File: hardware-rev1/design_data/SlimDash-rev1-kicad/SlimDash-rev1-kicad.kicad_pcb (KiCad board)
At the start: 2 copper layers, 157.1 x 131.5 mm, 70 parts

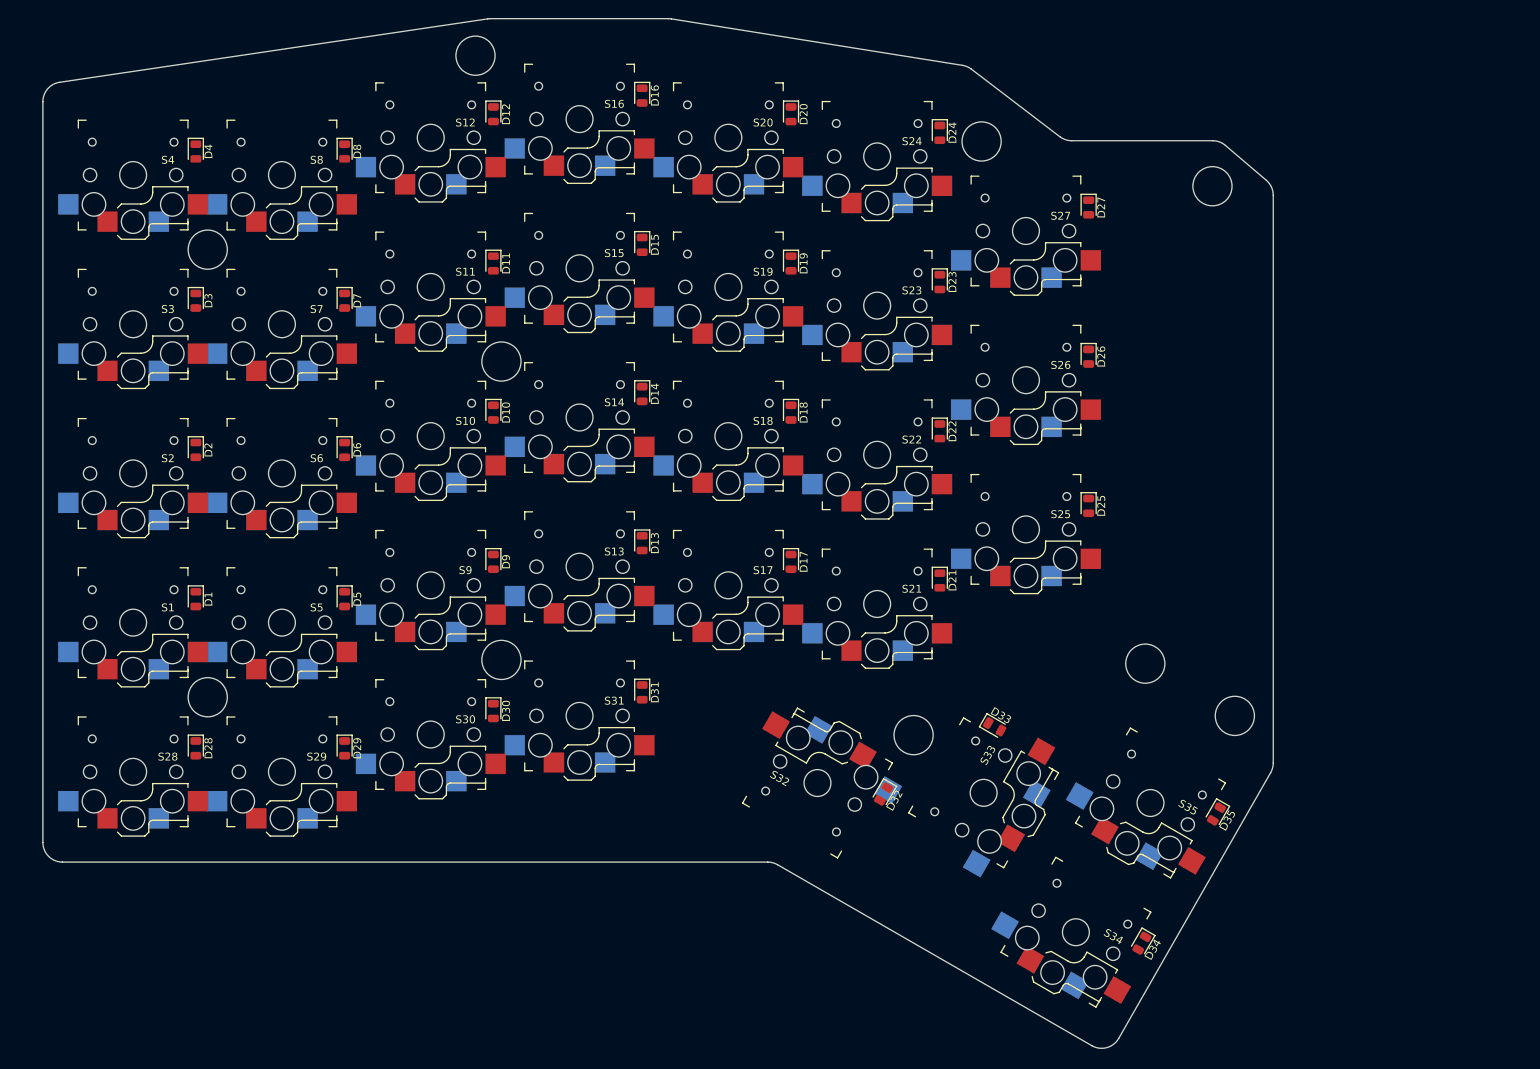
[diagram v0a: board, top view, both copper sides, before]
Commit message: fix some positioning and net labels
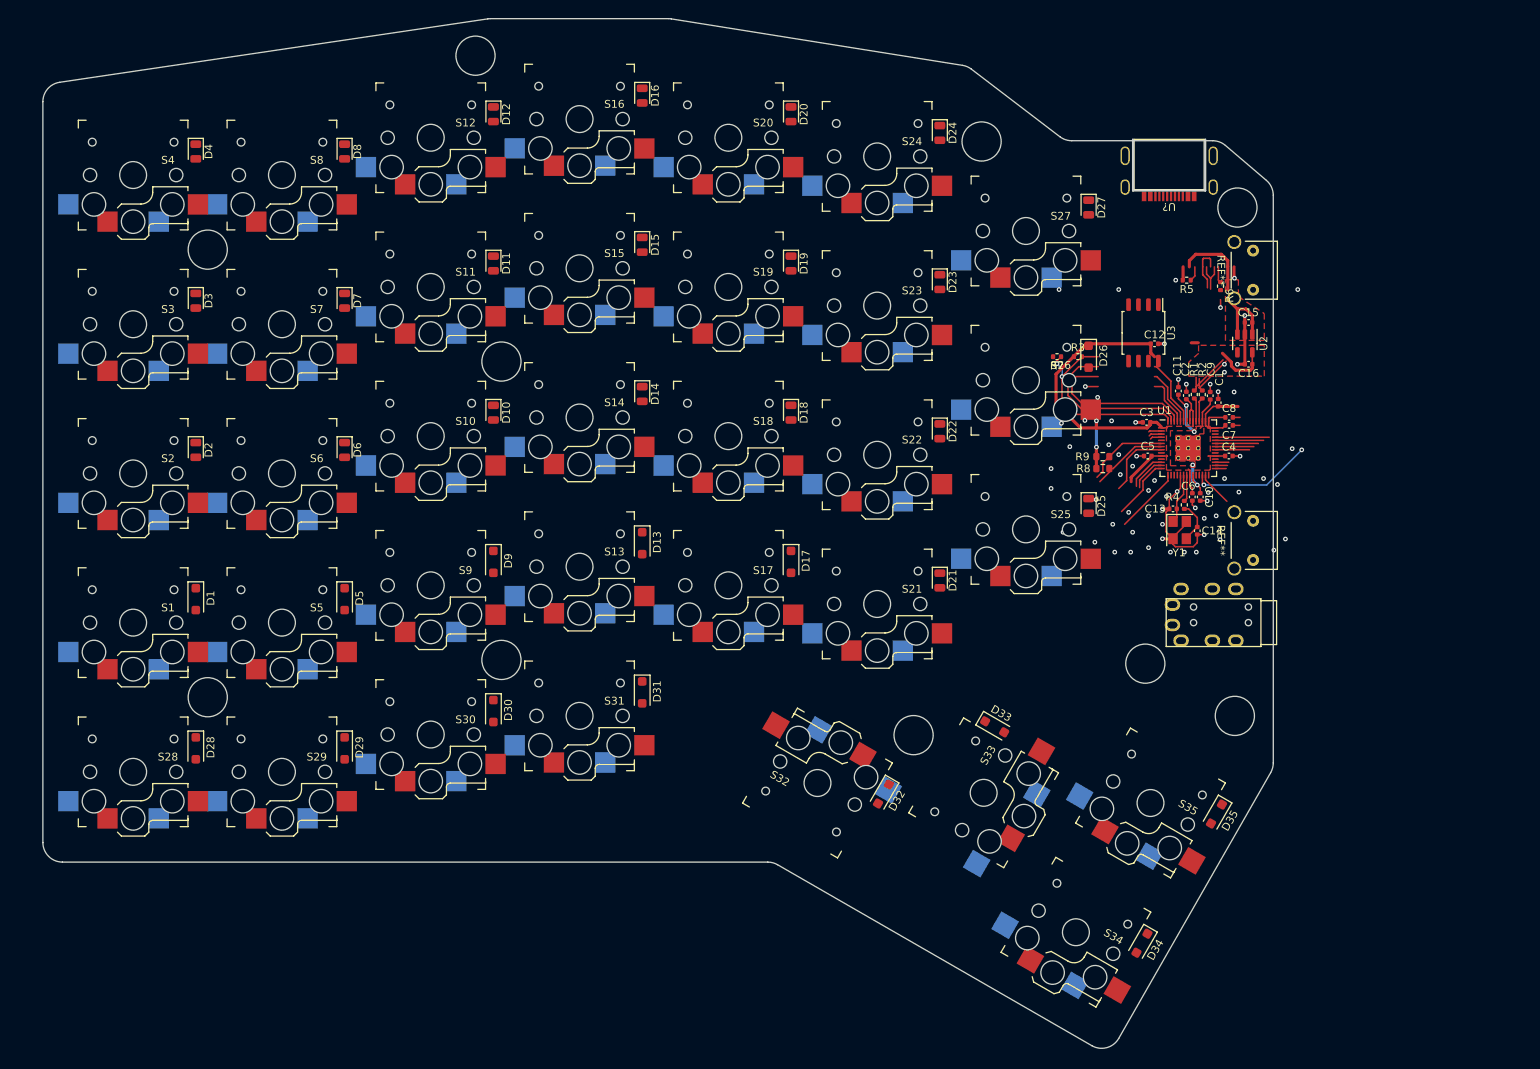
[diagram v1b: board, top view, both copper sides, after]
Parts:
- added C1: 1u, Capacitor_SMD:C_0402_1005Metric, F.Cu at (188.5, 71.9)
- added C10: 100n, Capacitor_SMD:C_0402_1005Metric, F.Cu at (186.3, 84.0)
- added C11: 100n, Capacitor_SMD:C_0402_1005Metric, F.Cu at (183.5, 70.4)
- added C12: 100n, Capacitor_SMD:C_0402_1005Metric, F.Cu at (180.4, 64.4)
- added C13: 30p, Capacitor_SMD:C_0402_1005Metric, F.Cu at (182.8, 85.5)
- added C14: 30p, Capacitor_SMD:C_0402_1005Metric, F.Cu at (185.9, 88.3)
- added C15: 1u, Capacitor_SMD:C_0402_1005Metric, F.Cu at (192.4, 61.7)
- added C16: 1u, Capacitor_SMD:C_0402_1005Metric, F.Cu at (192.4, 67.0)
- added C2: 100n, Capacitor_SMD:C_0402_1005Metric, F.Cu at (184.5, 71.0)
- added C3: 100n, Capacitor_SMD:C_0402_1005Metric, F.Cu at (179.4, 74.4)
- added C4: 100n, Capacitor_SMD:C_0402_1005Metric, F.Cu at (189.9, 78.7)
- added C5: 100n, Capacitor_SMD:C_0402_1005Metric, F.Cu at (179.6, 78.7)
- added C6: 100n, Capacitor_SMD:C_0402_1005Metric, F.Cu at (185.2, 84.0)
- added C7: 100n, Capacitor_SMD:C_0402_1005Metric, F.Cu at (189.9, 74.8)
- added C8: 100n, Capacitor_SMD:C_0402_1005Metric, F.Cu at (189.9, 73.8)
- added C9: 1u, Capacitor_SMD:C_0402_1005Metric, F.Cu at (187.5, 71.0)
- added R1: 27, Resistor_SMD:R_0402_1005Metric, F.Cu at (185.5, 70.9)
- added R2: 27, Resistor_SMD:R_0402_1005Metric, F.Cu at (186.5, 70.9)
- added R3: 10k, Resistor_SMD:R_0402_1005Metric, F.Cu at (170.6, 66.0)
- added R4: 1k, Resistor_SMD:R_0402_1005Metric, F.Cu at (184.2, 85.0)
- added R5: 5.1k, Resistor_SMD:R_0402_1005Metric, F.Cu at (184.5, 56.3)
- added R6: 5.1k, Resistor_SMD:R_0402_1005Metric, F.Cu at (188.8, 57.0)
- added R7: 1k, Resistor_SMD:R_0402_1005Metric, F.Cu at (168.0, 66.0)
- added R8: 4.7k, Resistor_SMD:R_0603_1608Metric, F.Cu at (173.8, 80.3)
- added R9: 4.7k, Resistor_SMD:R_0603_1608Metric, F.Cu at (173.8, 78.8)
- added REF**: SW_Tactile_Yushakobo 3x6x4.3mm, mzm_misc:SW_Tactile_Yushakobo 3x6x4.3mm, F.Cu at (193.0, 52.5)
- added REF**: TRRS-PJ-320A, Keebio-Parts:TRRS-PJ-320A, F.Cu at (194.0, 100.0)
- added REF**: SW_Tactile_Yushakobo 3x6x4.3mm, mzm_misc:SW_Tactile_Yushakobo 3x6x4.3mm, F.Cu at (193.0, 87.0)
- added REF**: TRRS-PJ-320A, Keebio-Parts:TRRS-PJ-320A, B.Cu at (194.0, 98.0)
- added U1: RP2040, RP2040:RP2040-QFN-56, F.Cu at (184.7, 77.7)
- added U2: TLV73333PDBV, Package_TO_SOT_SMD:SOT-23-5, F.Cu at (191.9, 64.3)
- added U3: W25Q128JVS, Package_SO:SOIC-8_5.23x5.23mm_P1.27mm, F.Cu at (179.0, 63.0)
- added U?: HRO_USB-C-SMD_TYPE-C-31-M-13C, mzm_LCSC:HRO_USB-C-SMD_TYPE-C-31-M-13C, F.Cu at (182.3, 43.0)
- added Y1: Crystal_GND24, Crystal:Crystal_SMD_3225-4Pin_3.2x2.5mm, F.Cu at (183.6, 88.2)
- D1, D13, D17, D26, D28, D29, D30, D31, D32, D33, D34, D35, D5, D9: footprint Diode_SMD:D_0805_2012Metric -> Diode_SMD:D_SOD-123F
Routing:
- net (no net): track 0.00 -> 415.9 mm, vias 0 -> 76
- added copper zone on F.Cu, net (none)
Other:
- outline, holes or cut-outs redrawn

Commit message: start planning for routing
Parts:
- removed R6: 5.1k, Resistor_SMD:R_0402_1005Metric
- removed R8: 4.7k, Resistor_SMD:R_0603_1608Metric
- removed the REF** at (193.0, 52.5)
- removed the REF** at (194.0, 100.0)
- removed the REF** at (193.0, 87.0)
- removed the REF** at (194.0, 98.0)
- removed U?: HRO_USB-C-SMD_TYPE-C-31-M-13C, mzm_LCSC:HRO_USB-C-SMD_TYPE-C-31-M-13C
- added REF**: SK6812-MINI-E, Keebio-Parts:SK6812-MINI-E, F.Cu at (126.0, 90.5)
- added REF**: TRRS-PJ-320A, Keebio-Parts:TRRS-PJ-320A, F.Cu at (195.8, 104.2)
- added REF**: TRRS-PJ-320A, Keebio-Parts:TRRS-PJ-320A, B.Cu at (195.8, 102.0)
- added SW_BOOT1: SW_PUSH, mzm_misc:SW_Tactile_Yushakobo 3x6x4.3mm, F.Cu at (192.8, 52.5)
- added SW_RST1: SW_PUSH, mzm_misc:SW_Tactile_Yushakobo 3x6x4.3mm, F.Cu at (192.8, 90.0)
- added USB1: HRO-TYPE-C-31-M-12, ai03-2725_Type-C:HRO-TYPE-C-31-M-12-Assembly, F.Cu at (180.8, 38.4)
- C1, C15, C16, C9: value 1u -> 100n
- C10, C2, C3, C5: value 100n -> 1u
- C11, C8: value 100n -> 30p
- C13, C14: value 30p -> 100n
- D10, D11, D12, D14, D15, D16, D18, D19, D2, D20, D21, D22, D23, D24, D25, D27, D3, D4, D6, D7, D8: footprint Diode_SMD:D_0805_2012Metric -> Diode_SMD:D_SOD-123F
- R1: value 27 -> 1k
- R3: value 10k -> 27
- R5: value 5.1k -> 10k
- R7: value 1k -> 5.1k
- R9: value 4.7k -> 5.1k; footprint Resistor_SMD:R_0603_1608Metric -> Resistor_SMD:R_0402_1005Metric
- U1: value RP2040 -> TLV73333PDBV; footprint RP2040:RP2040-QFN-56 -> Package_TO_SOT_SMD:SOT-23-5
- U2: value TLV73333PDBV -> RP2040; footprint Package_TO_SOT_SMD:SOT-23-5 -> RP2040:RP2040-QFN-56
- moved R7 48.5 mm to (210.5, 89.4), turned to 0 degrees
- moved C12 44.0 mm to (219.1, 85.4)
- moved R5 40.6 mm to (210.5, 87.5), turned to 0 degrees
- moved C13 39.7 mm to (222.0, 79.5)
- moved R9 38.8 mm to (210.5, 91.4), turned to 0 degrees
- moved C11 38.0 mm to (219.1, 83.4), turned to 0 degrees
- moved R3 37.1 mm to (200.5, 88.0)
- moved C14 36.7 mm to (222.0, 81.5), turned to 0 degrees
- moved C15 36.7 mm to (222.0, 83.4), turned to 0 degrees
- moved C5 36.7 mm to (216.2, 79.5), turned to 0 degrees
- moved C3 35.1 mm to (213.4, 83.4), turned to 0 degrees
- moved C16 34.8 mm to (222.0, 85.4), turned to 0 degrees
- moved C10 33.0 mm to (219.1, 81.5), turned to 0 degrees
- moved C9 32.7 mm to (219.1, 79.5), turned to 0 degrees
- moved C6 31.1 mm to (216.2, 81.5), turned to 0 degrees
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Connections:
- net ROW5 renamed ROW0
- C1 pad 1: (no net) -> +1V1
- C1 pad 2: (no net) -> GND
- C10 pad 1: (no net) -> +3V3
- C10 pad 2: (no net) -> GND
- C11 pad 1: (no net) -> Net-(C11-Pad1)
- C11 pad 2: (no net) -> GND
- C12 pad 1: (no net) -> +3V3
- C12 pad 2: (no net) -> GND
- C13 pad 1: (no net) -> +3V3
- C13 pad 2: (no net) -> GND
- C14 pad 1: (no net) -> +3V3
- C14 pad 2: (no net) -> GND
- C15 pad 1: (no net) -> +3V3
- C15 pad 2: (no net) -> GND
- C16 pad 1: (no net) -> +3V3
- C16 pad 2: (no net) -> GND
- C2 pad 1: (no net) -> +5V
- C2 pad 2: (no net) -> GND
- C3 pad 1: (no net) -> +1V1
- C3 pad 2: (no net) -> GND
- C4 pad 1: (no net) -> +1V1
- C4 pad 2: (no net) -> GND
- C5 pad 1: (no net) -> +3V3
- C5 pad 2: (no net) -> GND
- C6 pad 1: (no net) -> +3V3
- C6 pad 2: (no net) -> GND
- C7 pad 1: (no net) -> +3V3
- C7 pad 2: (no net) -> GND
- C8 pad 1: (no net) -> GND
- C8 pad 2: (no net) -> XIN
- C9 pad 1: (no net) -> +3V3
- C9 pad 2: (no net) -> GND
- D1 pad 1: ROW2 -> ROW3
- D10 pad 1: ROW3 -> ROW2
- D11 pad 1: ROW4 -> ROW1
- D13 pad 1: ROW2 -> ROW3
- D14 pad 1: ROW3 -> ROW2
- D15 pad 1: ROW4 -> ROW1
- D17 pad 1: ROW2 -> ROW3
- D18 pad 1: ROW3 -> ROW2
- D19 pad 1: ROW4 -> ROW1
- D2 pad 1: ROW3 -> ROW2
- D21 pad 1: ROW2 -> ROW3
- D22 pad 1: ROW3 -> ROW2
- D23 pad 1: ROW4 -> ROW1
- D25 pad 1: ROW3 -> ROW2
- D26 pad 1: ROW4 -> ROW1
- D28 pad 1: ROW1 -> ROW4
- D29 pad 1: ROW1 -> ROW4
- D3 pad 1: ROW4 -> ROW1
- D30 pad 1: ROW1 -> ROW4
- D31 pad 1: ROW1 -> ROW4
- D32 pad 1: ROW1 -> ROW4
- D33 pad 1: ROW1 -> ROW4
- D34 pad 1: ROW1 -> ROW4
- D35 pad 1: ROW2 -> ROW3
- D5 pad 1: ROW2 -> ROW3
- D6 pad 1: ROW3 -> ROW2
- D7 pad 1: ROW4 -> ROW1
- D9 pad 1: ROW2 -> ROW3
- R1 pad 1: (no net) -> Net-(C11-Pad1)
- R1 pad 2: (no net) -> XOUT
- R2 pad 1: (no net) -> USB_DP
- R2 pad 2: (no net) -> Net-(U2-USB_DP)
- R3 pad 1: (no net) -> USB_DM
- R3 pad 2: (no net) -> Net-(U2-USB_DM)
- R4 pad 1: (no net) -> QSPI_SS
- R4 pad 2: (no net) -> Net-(R4-Pad2)
- R5 pad 1: (no net) -> +3V3
- R5 pad 2: (no net) -> QSPI_SS
- R7 pad 1: (no net) -> Net-(USB1-CC2)
- R7 pad 2: (no net) -> GND
- R9 pad 1: (no net) -> Net-(USB1-CC1)
- R9 pad 2: (no net) -> GND
- S1 pad 1: COL1 -> COL0
- S10 pad 1: COL3 -> COL2
- S11 pad 1: COL3 -> COL2
- S12 pad 1: COL3 -> COL2
- S13 pad 1: COL4 -> COL3
- S14 pad 1: COL4 -> COL3
- S15 pad 1: COL4 -> COL3
- S16 pad 1: COL4 -> COL3
- S17 pad 1: COL5 -> COL4
- S18 pad 1: COL5 -> COL4
- S19 pad 1: COL5 -> COL4
- S2 pad 1: COL1 -> COL0
- S20 pad 1: COL5 -> COL4
- S21 pad 1: COL6 -> COL5
- S22 pad 1: COL6 -> COL5
- S23 pad 1: COL6 -> COL5
- S24 pad 1: COL6 -> COL5
- S25 pad 1: COL7 -> COL6
- S26 pad 1: COL7 -> COL6
- S27 pad 1: COL7 -> COL6
- S28 pad 1: COL1 -> COL0
- S29 pad 1: COL2 -> COL1
- S3 pad 1: COL1 -> COL0
- S30 pad 1: COL3 -> COL2
- S31 pad 1: COL4 -> COL3
- S32 pad 1: COL5 -> COL4
- S33 pad 1: COL6 -> COL5
- S34 pad 1: COL7 -> COL6
- S35 pad 1: COL7 -> COL6
- S4 pad 1: COL1 -> COL0
- S5 pad 1: COL2 -> COL1
- S6 pad 1: COL2 -> COL1
- S7 pad 1: COL2 -> COL1
- S8 pad 1: COL2 -> COL1
- S9 pad 1: COL3 -> COL2
- U1 pad 1: (no net) -> +5V
- U1 pad 2: (no net) -> GND
- U1 pad 3: (no net) -> +5V
- U1 pad 4: (no net) -> unconnected-(U1-NC-Pad4)
- U1 pad 5: (no net) -> +3V3
- U2 pad 1: (no net) -> +3V3
- U2 pad 2: (no net) -> unconnected-(U2-GPIO0-Pad2)
- U2 pad 3: (no net) -> unconnected-(U2-GPIO1-Pad3)
- U2 pad 4: (no net) -> unconnected-(U2-GPIO2-Pad4)
- U2 pad 5: (no net) -> unconnected-(U2-GPIO3-Pad5)
- U3 pad 1: (no net) -> QSPI_SS
- U3 pad 2: (no net) -> QSPI_SD1
- U3 pad 3: (no net) -> QSPI_SD2
- U3 pad 4: (no net) -> GND
- U3 pad 5: (no net) -> QSPI_SD0
- U3 pad 6: (no net) -> QSPI_SCLK
- U3 pad 7: (no net) -> QSPI_SD3
- U3 pad 8: (no net) -> +3V3
- Y1 pad 1: (no net) -> XIN
- Y1 pad 2: (no net) -> GND
- Y1 pad 3: (no net) -> Net-(C11-Pad1)
- Y1 pad 4: (no net) -> GND
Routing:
- net (no net): track 415.9 -> 0.00 mm, vias 76 -> 0
- net ROW4: track 0.00 -> 196.0 mm, vias 0 -> 2
- net COL2: track 0.00 -> 188.5 mm
- net ROW3: track 0.00 -> 176.9 mm
- net COL3: track 0.00 -> 170.8 mm
- net COL4: track 0.00 -> 167.1 mm
- net COL0: track 0.00 -> 153.4 mm
- net COL1: track 0.00 -> 139.4 mm
- net COL5: track 0.00 -> 136.8 mm
- net ROW2: track 0.00 -> 132.2 mm
- net COL6: track 0.00 -> 99.7 mm
- net ROW1: track 0.00 -> 77.5 mm
- net ROW0: track 0.00 -> 76.7 mm
- net +3V3: track 0.00 -> 42.0 mm
- net QSPI_SS: track 0.00 -> 29.9 mm
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- removed copper zone on F.Cu, net (none)
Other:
- outline, holes or cut-outs redrawn

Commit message: add more components to design data
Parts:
- removed the REF** at (126.0, 90.5)
- removed the REF** at (195.8, 104.2)
- removed the REF** at (195.8, 102.0)
- added J1: AudioJack4, Keebio-Parts:TRRS-PJ-320A, F.Cu at (195.4, 103.9)
- added J2: AudioJack4, Keebio-Parts:TRRS-PJ-320A, B.Cu at (195.4, 101.8)
- added LED1: , mzm_misc:SK6812-MINI-E_Reversible, F.Cu at (50.0, 95.3)
- added LED10: , mzm_misc:SK6812-MINI-E_Reversible, F.Cu at (88.0, 71.5)
- added LED11: , mzm_misc:SK6812-MINI-E_Reversible, F.Cu at (88.0, 52.4)
- added LED12: , mzm_misc:SK6812-MINI-E_Reversible, F.Cu at (88.0, 33.4)
- added LED13: , mzm_misc:SK6812-MINI-E_Reversible, F.Cu at (107.0, 88.2)
- added LED14: , mzm_misc:SK6812-MINI-E_Reversible, F.Cu at (107.0, 69.1)
- added LED15: , mzm_misc:SK6812-MINI-E_Reversible, F.Cu at (107.0, 50.1)
- added LED16: , mzm_misc:SK6812-MINI-E_Reversible, F.Cu at (107.0, 31.0)
- added LED17: , mzm_misc:SK6812-MINI-E_Reversible, F.Cu at (126.0, 90.5)
- added LED18: , mzm_misc:SK6812-MINI-E_Reversible, F.Cu at (126.0, 71.5)
- added LED19: , mzm_misc:SK6812-MINI-E_Reversible, F.Cu at (126.0, 52.4)
- added LED2: , mzm_misc:SK6812-MINI-E_Reversible, F.Cu at (50.0, 76.2)
- added LED20: , mzm_misc:SK6812-MINI-E_Reversible, F.Cu at (126.0, 33.4)
- added LED21: , mzm_misc:SK6812-MINI-E_Reversible, F.Cu at (145.0, 92.9)
- added LED22: , mzm_misc:SK6812-MINI-E_Reversible, F.Cu at (145.0, 73.9)
- added LED23: , mzm_misc:SK6812-MINI-E_Reversible, F.Cu at (145.0, 54.8)
- added LED24: , mzm_misc:SK6812-MINI-E_Reversible, F.Cu at (145.0, 35.8)
- added LED25: , mzm_misc:SK6812-MINI-E_Reversible, F.Cu at (164.0, 83.4)
- added LED26: , mzm_misc:SK6812-MINI-E_Reversible, F.Cu at (164.0, 64.3)
- added LED27: , mzm_misc:SK6812-MINI-E_Reversible, F.Cu at (164.0, 45.3)
- added LED28: , mzm_misc:SK6812-MINI-E_Reversible, F.Cu at (50.0, 114.3)
- added LED29: , mzm_misc:SK6812-MINI-E_Reversible, F.Cu at (69.0, 114.3)
- added LED3: , mzm_misc:SK6812-MINI-E_Reversible, F.Cu at (50.0, 57.2)
- added LED30: , mzm_misc:SK6812-MINI-E_Reversible, F.Cu at (88.0, 109.6)
- added LED31: , mzm_misc:SK6812-MINI-E_Reversible, F.Cu at (107.0, 107.2)
- added LED32: , mzm_misc:SK6812-MINI-E_Reversible, F.Cu at (139.7, 116.4)
- added LED33: , mzm_misc:SK6812-MINI-E_Reversible, F.Cu at (154.5, 119.4)
- added LED34: , mzm_misc:SK6812-MINI-E_Reversible, F.Cu at (172.7, 135.5)
- added LED35: , mzm_misc:SK6812-MINI-E_Reversible, F.Cu at (182.3, 119.0)
- added LED4: , mzm_misc:SK6812-MINI-E_Reversible, F.Cu at (50.0, 38.1)
- added LED5: , mzm_misc:SK6812-MINI-E_Reversible, F.Cu at (69.0, 95.3)
- added LED6: , mzm_misc:SK6812-MINI-E_Reversible, F.Cu at (69.0, 76.2)
- added LED7: , mzm_misc:SK6812-MINI-E_Reversible, F.Cu at (69.0, 57.2)
- added LED8: , mzm_misc:SK6812-MINI-E_Reversible, F.Cu at (69.0, 38.1)
- added LED9: , mzm_misc:SK6812-MINI-E_Reversible, F.Cu at (88.0, 90.5)
- added REF**: Stabilizer_MX_2u, daprice_keyswitches:Stabilizer_MX_2u, F.Cu at (158.6, 121.7)
- moved R4 36.8 mm to (214.4, 73.0)
- moved R3 22.0 mm to (214.4, 71.0)
- moved C1 13.1 mm to (217.3, 67.0)
- moved C13 13.1 mm to (225.9, 67.0)
- moved C14 13.1 mm to (225.9, 69.0)
- moved C15 13.1 mm to (225.9, 70.9)
- moved C16 13.1 mm to (225.9, 72.9)
- moved C2 13.1 mm to (217.3, 69.0)
- moved C3 13.1 mm to (217.3, 70.9)
- moved C4 13.1 mm to (217.3, 72.9)
- moved C5 13.1 mm to (220.1, 67.0)
- moved C6 13.1 mm to (220.1, 69.0)
- moved C7 13.1 mm to (220.1, 70.9)
- moved C8 13.1 mm to (220.1, 72.9)
- moved R1 13.1 mm to (214.4, 67.0)
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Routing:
- net ROW4: track 196.0 -> 0.00 mm, vias 2 -> 0
- net COL2: track 188.5 -> 0.00 mm
- net ROW3: track 176.9 -> 0.00 mm
- net COL3: track 170.8 -> 0.00 mm
- net COL4: track 167.1 -> 0.00 mm
- net COL0: track 153.4 -> 0.00 mm
- net COL1: track 139.4 -> 0.00 mm
- net COL5: track 136.8 -> 0.00 mm
- net ROW2: track 132.2 -> 0.00 mm
- net COL6: track 99.7 -> 0.00 mm
- net ROW1: track 77.5 -> 0.00 mm
- net ROW0: track 76.7 -> 0.00 mm
- net +3V3: track 42.0 -> 2.51 mm
- net QSPI_SS: track 29.9 -> 0.00 mm
- net QSPI_SD1: track 26.4 -> 0.00 mm
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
